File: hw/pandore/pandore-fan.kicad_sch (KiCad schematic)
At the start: 0 parts

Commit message: lcd control circuit added fan interface added rgba output pinout for management mcu accessories done
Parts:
- added C234: ${Capacitance}, ${Voltage}, ${Dielectric}, reekilib_cap:CAPC1005, symbol reekilib_cap:cap
- added D28: ${Vr}, ${Io}, ${Vf}, reekilib_sod:sod-123, symbol reekilib_dio:diode
- added J27: hdr-1x4, reekilib_con:molex_0470531000, symbol reekilib_con:hdr-1x4
- added R198, R200, R201: ${Resistance}, ${Tolerance}, ${Power}, reekilib_res:RESC1005, symbol reekilib_res:res
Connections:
- new net: D28.2 (A), J27.3, R198.2, R200.2
- new net: J27.4, R201.2
- new net FANCPU.PWM: R201.1
- new net FANCPU.TAC: R200.1
- new net V5: C234.2, D28.1 (C), J27.2, R198.1
- new net VSS: C234.1, J27.1

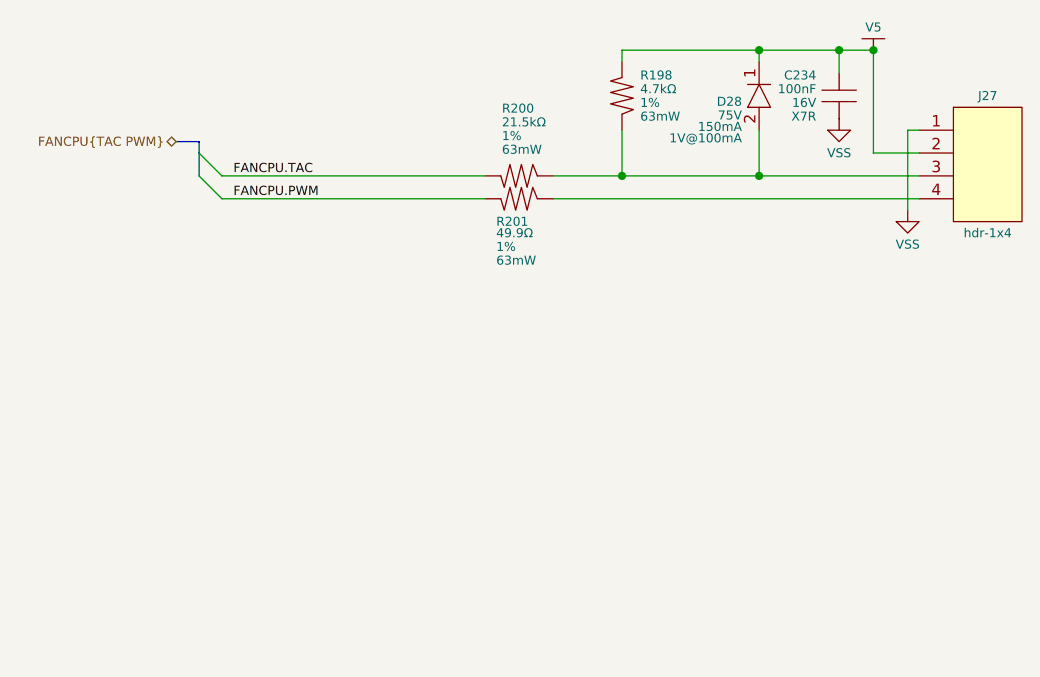
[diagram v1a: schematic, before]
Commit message: more routing/placement done added 5v load switch 1A each added second fan circuit redone all diffpair routing following new stackup calc added all (?) missing connectors to unused pins
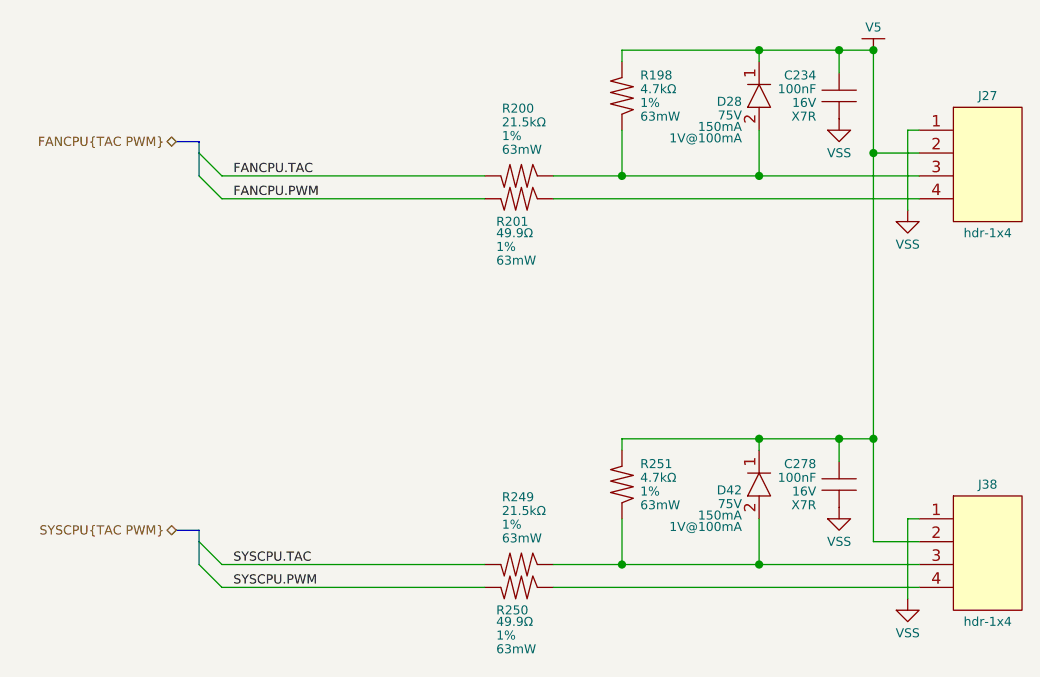
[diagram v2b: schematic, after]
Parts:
- added C278: ${Capacitance}, ${Voltage}, ${Dielectric}, reekilib_cap:CAPC1005, symbol reekilib_cap:cap
- added D42: ${Vr}, ${Io}, ${Vf}, reekilib_sod:sod-123, symbol reekilib_dio:diode
- added J38: hdr-1x4, reekilib_con:molex_0470531000, symbol reekilib_con:hdr-1x4
- added R249, R250, R251: ${Resistance}, ${Tolerance}, ${Power}, reekilib_res:RESC1005, symbol reekilib_res:res
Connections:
- net V5: now also C278.2, D42.1 (C), J38.2, R251.1
- net VSS: now also C278.1, J38.1
- new net: D42.2 (A), J38.3, R249.2, R251.2
- new net: J38.4, R250.2
- new net SYSCPU.PWM: R250.1
- new net SYSCPU.TAC: R249.1

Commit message: finished adding mpn,mfg to all parts, finished routing placement
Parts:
- C234, C278: MFG2 Samsung Electro-Mechanics -> (none); MFG3 Taiyo Yuden -> (none); MPN2 CL05B104KA5NNNC -> (none); MPN3 EMK105B7104KV-F -> (none); Voltage 16V -> 25V
- R198, R251: Link (none) -> https://yageogroup.com/products/Resistors/part/RC0402FR-074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; MFG (none) -> YAGEO; MPN (none) -> RC0402FR-074K7L
- R200, R249: Link (none) -> https://yageogroup.com/products/Resistors/part/RC0402FR-072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; MFG (none) -> YAGEO; MPN (none) -> RC0402FR-0721KL; Resistance 21.5kΩ -> 21kΩ
- R201, R250: Link (none) -> https://yageogroup.com/products/Resistors/part/RC0402FR-074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; MFG (none) -> YAGEO; MPN (none) -> RC0402FR-0749R9L
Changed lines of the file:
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@@
 			)
 		)
-		(property "Voltage" "16V"
+		(property "Voltage" "25V"
 			(at 205.74 49.022 0)
 			(do_not_autoplace yes)
@@
 			)
 		)
-		(property "MPN2" "CL05B104KA5NNNC"
+		(property "MPN2" ""
 			(at 208.28 68.58 0)
 			(do_not_autoplace yes)
@@
 			)
 		)
-		(property "MFG2" "Samsung Electro-Mechanics"
+		(property "MFG2" ""
 			(at 196.342 68.58 0)
 			(do_not_autoplace yes)
@@
 			)
 		)
-		(property "MPN3" "EMK105B7104KV-F"
+		(property "MPN3" ""
 			(at 208.28 70.104 0)
 			(do_not_autoplace yes)
@@
 			)
 		)
-		(property "MFG3" "Taiyo Yuden"
+		(property "MFG3" ""
 			(at 196.342 70.104 0)
 			(do_not_autoplace yes)
@@
 			)
 		)
-		(property "Datasheet" ""
+		(property "Datasheet" "https://yageogroup.com/content/datasheet/asset/file/PYU-RC_GROUP_51_ROHS_L"
 			(at 186.944 100.33 0)
 			(do_not_autoplace yes)
@@
 			)
 		)
-		(property "Link" ""
+		(property "Link" "https://yageogroup.com/products/Resistors/part/RC0402FR-0721KL"
 			(at 188.468 100.076 0)
 			(do_not_autoplace yes)
@@
 			)
 		)
-		(property "Resistance" "21.5kΩ"
+		(property "Resistance" "21kΩ"
 			(at 170.815 94.361 90)
 			(do_not_autoplace yes)
@@
 			)
 		)
-		(property "MPN" ""
+		(property "MPN" "RC0402FR-0721KL"
 			(at 190.5 100.33 0)
 			(do_not_autoplace yes)
@@
 			)
 		)
-		(property "MFG" ""
+		(property "MFG" "YAGEO"
 			(at 190.246 86.36 0)
 			(do_not_autoplace yes)
@@
 			)
 		)
-		(property "Datasheet" ""
+		(property "Datasheet" "https://yageogroup.com/content/datasheet/asset/file/PYU-RC_GROUP_51_ROHS_L"
 			(at 186.944 102.87 0)
 			(do_not_autoplace yes)
@@
 			)
 		)
-		(property "MPN" ""
+		(property "MPN" "RC0402FR-0749R9L"
 			(at 190.5 102.87 0)
 			(do_not_autoplace yes)
@@
 			)
 		)
-		(property "MFG" ""
+		(property "MFG" "YAGEO"
 			(at 190.246 88.9 0)
 			(do_not_autoplace yes)
@@
 			)
 		)
-		(property "Link" ""
+		(property "Link" "https://yageogroup.com/products/Resistors/part/RC0402FR-0749R9L"
 			(at 190.5 59.055 0)
 			(do_not_autoplace yes)
@@
 			)
 		)
-		(property "Voltage" "16V"
+		(property "Voltage" "25V"
 			(at 205.74 92.202 0)
 			(do_not_autoplace yes)
@@
 			)
 		)
-		(property "MPN2" "CL05B104KA5NNNC"
+		(property "MPN2" ""
 			(at 208.28 111.76 0)
 			(do_not_autoplace yes)
@@
 			)
 		)
-		(property "MFG2" "Samsung Electro-Mechanics"
+		(property "MFG2" ""
 			(at 196.342 111.76 0)
 			(do_not_autoplace yes)
@@
 			)
 		)
-		(property "MPN3" "EMK105B7104KV-F"
+		(property "MPN3" ""
 			(at 208.28 113.284 0)
 			(do_not_autoplace yes)
@@
 			)
 		)
-		(property "MFG3" "Taiyo Yuden"
+		(property "MFG3" ""
 			(at 196.342 113.284 0)
 			(do_not_autoplace yes)
@@
 			)
 		)
-		(property "Datasheet" ""
+		(property "Datasheet" "https://yageogroup.com/content/datasheet/asset/file/PYU-RC_GROUP_51_ROHS_L"
 			(at 186.944 57.15 0)
 			(do_not_autoplace yes)
@@
 			)
 		)
-		(property "Link" ""
+		(property "Link" "https://yageogroup.com/products/Resistors/part/RC0402FR-0721KL"
 			(at 188.468 56.896 0)
 			(do_not_autoplace yes)
@@
 			)
 		)
-		(property "Resistance" "21.5kΩ"
+		(property "Resistance" "21kΩ"
 			(at 170.815 51.181 90)
 			(do_not_autoplace yes)
@@
 			)
 		)
-		(property "MPN" ""
+		(property "MPN" "RC0402FR-0721KL"
 			(at 190.5 57.15 0)
 			(do_not_autoplace yes)
@@
 			)
 		)
-		(property "MFG" ""
+		(property "MFG" "YAGEO"
 			(at 190.246 43.18 0)
 			(do_not_autoplace yes)
@@
 			)
 		)
-		(property "Datasheet" ""
+		(property "Datasheet" "https://yageogroup.com/content/datasheet/asset/file/PYU-RC_GROUP_51_ROHS_L"
 			(at 184.15 62.484 0)
 			(do_not_autoplace yes)
@@
 			)
 		)
-		(property "Link" ""
+		(property "Link" "https://yageogroup.com/products/Resistors/part/RC0402FR-074K7L"
 			(at 184.404 64.008 0)
 			(do_not_autoplace yes)
@@
 			)
 		)
-		(property "MPN" ""
+		(property "MPN" "RC0402FR-074K7L"
 			(at 184.15 66.04 0)
 			(do_not_autoplace yes)
@@
 			)
 		)
-		(property "MFG" ""
+		(property "MFG" "YAGEO"
 			(at 198.12 65.786 0)
 			(do_not_autoplace yes)
@@
 			)
 		)
-		(property "Datasheet" ""
+		(property "Datasheet" "https://yageogroup.com/content/datasheet/asset/file/PYU-RC_GROUP_51_ROHS_L"
 			(at 184.15 105.664 0)
 			(do_not_autoplace yes)
@@
 			)
 		)
-		(property "Link" ""
+		(property "Link" "https://yageogroup.com/products/Resistors/part/RC0402FR-074K7L"
 			(at 184.404 107.188 0)
 			(do_not_autoplace yes)
@@
 			)
 		)
-		(property "MPN" ""
+		(property "MPN" "RC0402FR-074K7L"
 			(at 184.15 109.22 0)
 			(do_not_autoplace yes)
@@
 			)
 		)
-		(property "MFG" ""
+		(property "MFG" "YAGEO"
 			(at 198.12 108.966 0)
 			(do_not_autoplace yes)
@@
 			)
 		)
-		(property "Datasheet" ""
+		(property "Datasheet" "https://yageogroup.com/content/datasheet/asset/file/PYU-RC_GROUP_51_ROHS_L"
 			(at 186.944 59.69 0)
 			(do_not_autoplace yes)
@@
 			)
 		)
-		(property "MPN" ""
+		(property "MPN" "RC0402FR-0749R9L"
 			(at 190.5 59.69 0)
 			(do_not_autoplace yes)
@@
 			)
 		)
-		(property "MFG" ""
+		(property "MFG" "YAGEO"
 			(at 190.246 45.72 0)
 			(do_not_autoplace yes)
@@
 			)
 		)
-		(property "Link" ""
+		(property "Link" "https://yageogroup.com/products/Resistors/part/RC0402FR-0749R9L"
 			(at 190.5 15.875 0)
 			(do_not_autoplace yes)
